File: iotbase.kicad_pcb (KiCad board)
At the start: 2 copper layers, 57.6 x 72.5 mm, 36 parts, among them J1 USB_C_Receptacle_USB2.0, J2 RCWL-0516, SW1 Reset, SW2 Boot, U1 AMS1117-3.3, U2 STF202-22T1G, U3 ESP32-C3-WROOM-02, U4 BME280, U5 GPIO Connector, U6 Connector_ESProg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

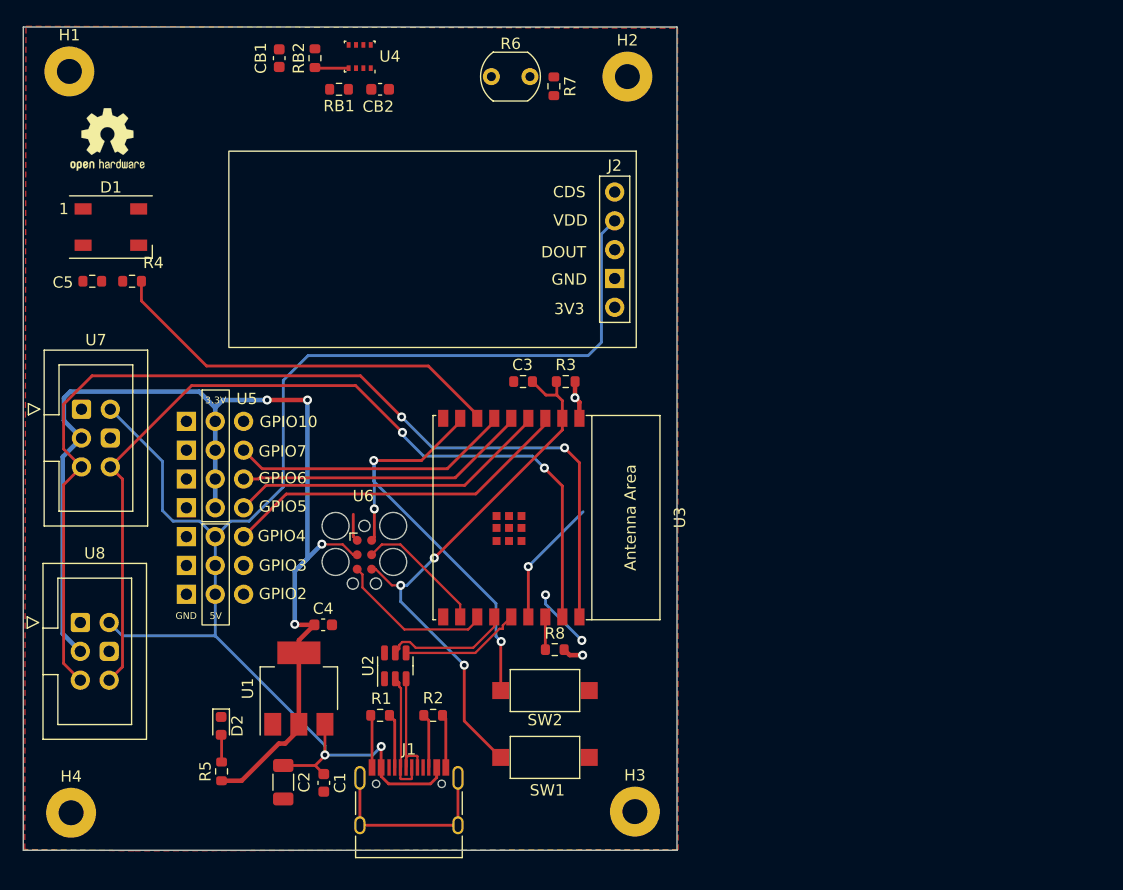
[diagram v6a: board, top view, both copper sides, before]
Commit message: updates routes
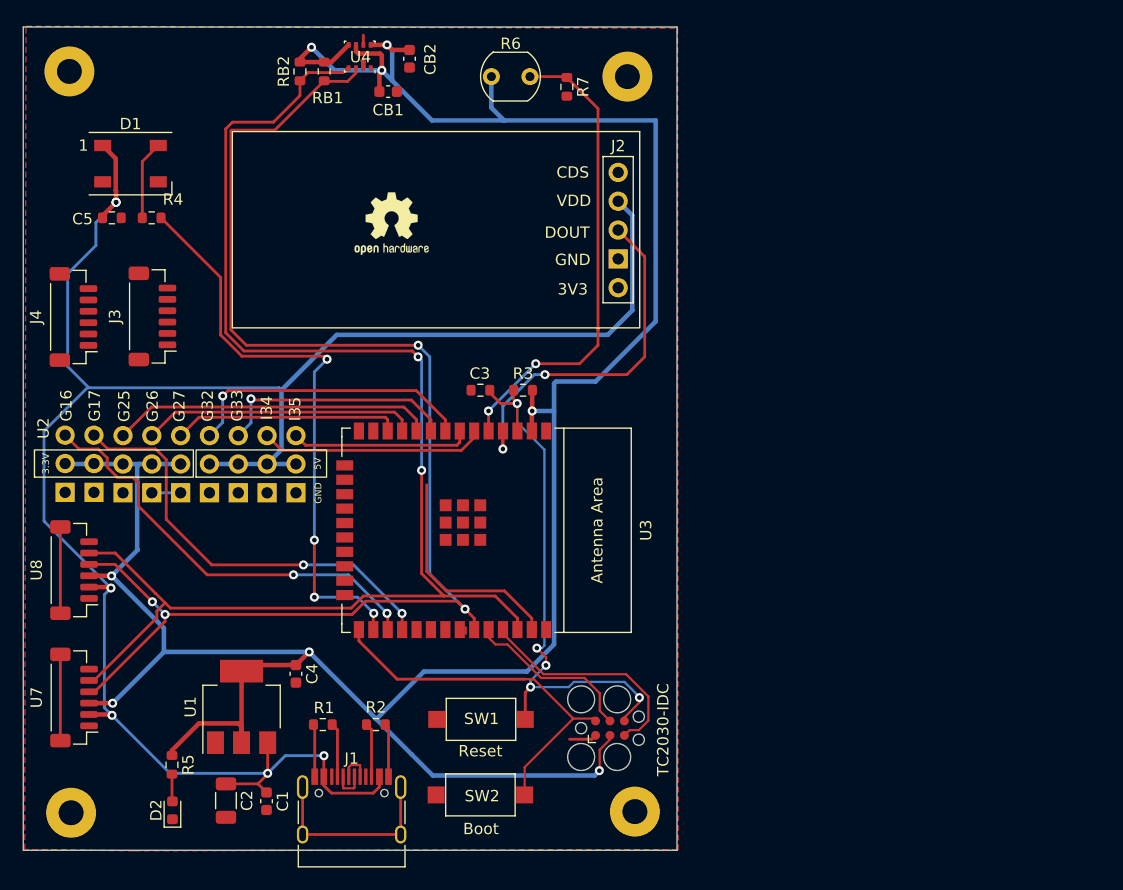
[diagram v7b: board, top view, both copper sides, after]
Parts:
- removed R8: 10kΩ, Resistor_SMD:R_0603_1608Metric
- removed U5: GPIO Connector, 0_Project:Connector_IoT_GPIO
- added J3: HSPI, Connector_JST:JST_SH_BM06B-SRSS-TB_1x06-1MP_P1.00mm_Vertical, F.Cu at (100.0, 83.0)
- added J4: VSPI, Connector_JST:JST_SH_BM06B-SRSS-TB_1x06-1MP_P1.00mm_Vertical, F.Cu at (93.1, 83.1)
- U2: value STF202-22T1G -> Connector_IoT_GPIO; footprint Package_TO_SOT_SMD:SOT-23-6 -> 0_Project:Connector_IoT_GPIO
- U3: value ESP32-C3-WROOM-02 -> ESP32-WROOM-E; footprint Espressif:ESP32-C3-WROOM-02 -> Espressif:ESP32-WROOM-32E
- U7, U8: footprint 0_Project:IDC-Header_2x03_P2.54mm_I2C -> Connector_JST:JST_SH_BM06B-SRSS-TB_1x06-1MP_P1.00mm_Vertical
- moved U2 38.9 mm to (89.1, 92.2)
- moved U6 26.5 mm to (140.3, 119.3), turned to 0 degrees
- moved REF** 26.1 mm to (121.1, 74.8)
- moved U7 25.4 mm to (93.1, 116.6), turned to 90 degrees
- moved SW2 10.8 mm to (128.9, 125.2), turned to 0 degrees
- moved CB1 10.0 mm to (120.8, 63.2), turned to 0 degrees
- moved D2 8.58 mm to (101.8, 126.5), turned to 90 degrees
- moved SW1 6.56 mm to (129.0, 118.5), turned to 0 degrees
- moved U3 5.89 mm to (127.7, 101.9)
- moved D1 5.85 mm to (98.1, 69.5)
- moved C5 5.85 mm to (96.5, 74.3)
- moved R4 5.85 mm to (100.0, 74.3)
- moved C1 5.30 mm to (110.1, 125.7)
- moved C2 5.30 mm to (106.5, 125.7)
- moved U1 5.30 mm to (107.9, 117.4)
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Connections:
- C3 pad 1: EN -> RESET
- J1 pad A6: D_IN+ -> unconnected-(J1-PadA6)
- J1 pad A7: D_IN- -> unconnected-(J1-PadA7)
- J1 pad B6: D_IN+ -> unconnected-(J1-PadB6)
- J1 pad B7: D_IN- -> unconnected-(J1-PadB7)
- J2 pad 3: GPIO3 -> IO36
- R3 pad 2: EN -> RESET
- R4 pad 1: GPIO8 -> GPIO4
- R6 pad 2: GPIO2 -> IO39
- R7 pad 1: GPIO2 -> IO39
- SW1 pad 2: EN -> RESET
- U2 pad 1: VBUS -> GND
- U2 pad 2: D_IN- -> +3V3
- U2 pad 3: D_IN+ -> VBUS
- U2 pad 6: GND -> IO35
- U3 pad 1: +3V3 -> GND
- U3 pad 10: GPIO10 -> GPIO25
- U3 pad 11: RXD -> GPIO26
- U3 pad 12: TXD -> GPIO27
- U3 pad 13: D- -> GPIO14
- U3 pad 14: D+ -> GPIO12
- U3 pad 15: GPIO3 -> GND
- U3 pad 16: GPIO2 -> GPIO13
- U3 pad 17: SCL -> unconnected-(U3-Pad17)
- U3 pad 18: SDA -> unconnected-(U3-Pad18)
- U3 pad 19: GND -> unconnected-(U3-Pad19)
- U3 pad 2: EN -> +3V3
- U3 pad 3: GPIO4 -> RESET
- U3 pad 4: GPIO5 -> IO36
- U3 pad 5: GPIO6 -> IO39
- U3 pad 6: GPIO7 -> IO34
- U3 pad 7: GPIO8 -> IO35
- U3 pad 8: BOOT -> GPIO32
- U3 pad 9: GND -> GPIO33
- U6 pad 6: EN -> RESET
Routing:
- net +3V3: track 108.1 -> 243.3 mm, vias 6 -> 8
- net RESET: track 0.00 -> 50.3 mm, vias 0 -> 5
- net EN: track 49.5 -> 0.00 mm, vias 3 -> 0
- net VBUS: track 129.5 -> 178.1 mm, vias 2 -> 6
- net IO39: track 0.00 -> 42.7 mm, vias 0 -> 2
- net SCL: track 81.0 -> 123.5 mm
- net GPIO17: track 0.00 -> 38.2 mm, vias 0 -> 2
- net GPIO16: track 0.00 -> 38.0 mm, vias 0 -> 2
- net GPIO8: track 35.8 -> 0.00 mm
- net IO36: track 0.00 -> 32.0 mm, vias 0 -> 2
- net SDA: track 89.5 -> 120.9 mm, vias 2 -> 4
- net GPIO5: track 28.5 -> 0.00 mm
- net GPIO25: track 0.00 -> 28.4 mm
- net GPIO6: track 26.1 -> 0.00 mm
- net GPIO32: track 0.00 -> 25.9 mm, vias 0 -> 1
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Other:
- board text added: "Boot"
- board text added: "Reset"
- board text added: "TC2030-IDC"

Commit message: updates additional routes
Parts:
- moved J4 27.0 mm to (106.6, 106.4)
- moved U2 20.9 mm to (97.8, 73.2), turned to 0 degrees
- moved J3 13.7 mm to (106.6, 95.0)
- moved C5 9.71 mm to (103.5, 67.6), turned to 90 degrees
- moved R4 4.76 mm to (103.5, 71.1), turned to 90 degrees
- moved D1 0.16 mm to (98.1, 69.4)
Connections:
- J3 pad 3: GPIO14 -> GPIO15
- J3 pad 4: GPIO12 -> GPIO13
- J3 pad 5: GPIO13 -> GPIO12
- J3 pad 6: GPIO15 -> GPIO14
- J4 pad 3: GPIO5 -> GPIO19
- J4 pad 5: GPIO19 -> GPIO5
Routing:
- net +3V3: track 243.3 -> 276.9 mm, vias 8 -> 10
- net GPIO19: track 0.00 -> 22.5 mm, vias 0 -> 2
- net GPIO18: track 0.00 -> 20.9 mm, vias 0 -> 2
- net GPIO5: track 0.00 -> 19.8 mm, vias 0 -> 2
- net GPIO15: track 0.00 -> 18.3 mm
- net IO35: track 15.9 -> 33.3 mm, vias 0 -> 2
- net VBUS: track 178.1 -> 162.9 mm, vias 6 -> 5
- net IO34: track 19.8 -> 34.4 mm, vias 0 -> 2
- net GPIO14: track 0.00 -> 12.7 mm
- net GPIO16: track 38.0 -> 50.4 mm
- net GPIO17: track 38.2 -> 50.0 mm
- net GPIO33: track 21.3 -> 32.2 mm, vias 1 -> 2
- net GPIO12: track 0.00 -> 10.4 mm
- net GPIO13: track 0.00 -> 10.2 mm
- net GPIO32: track 25.9 -> 36.1 mm, vias 1 -> 2
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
